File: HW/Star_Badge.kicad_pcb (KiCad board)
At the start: 2 copper layers, 180 x 171.6 mm, 55 parts, among them J1 AVR-ISP-6, J2 10118194-0001LF, Q1 Q_NMOS_DGS, Q2 Q_PMOS_DGS, U1 ATTINY861-15XD, U2 TPS613221ADBVT, U3 AP7363-33D-13, X1 Badgelife_sao_connector_v169b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, X2 Badgelife_sao_connector_v169b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, X3 Badgelife_sao_connector_v169b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

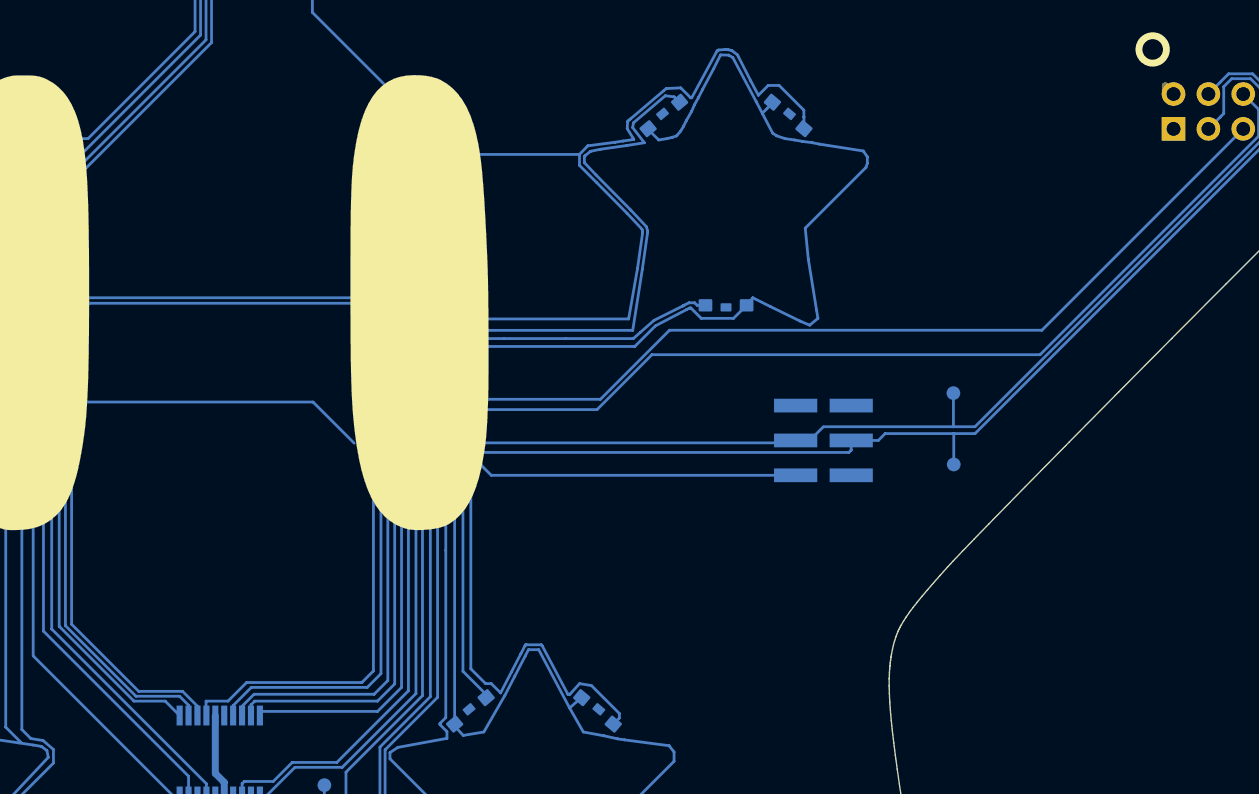
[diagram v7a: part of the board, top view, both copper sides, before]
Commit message: RESET wrired
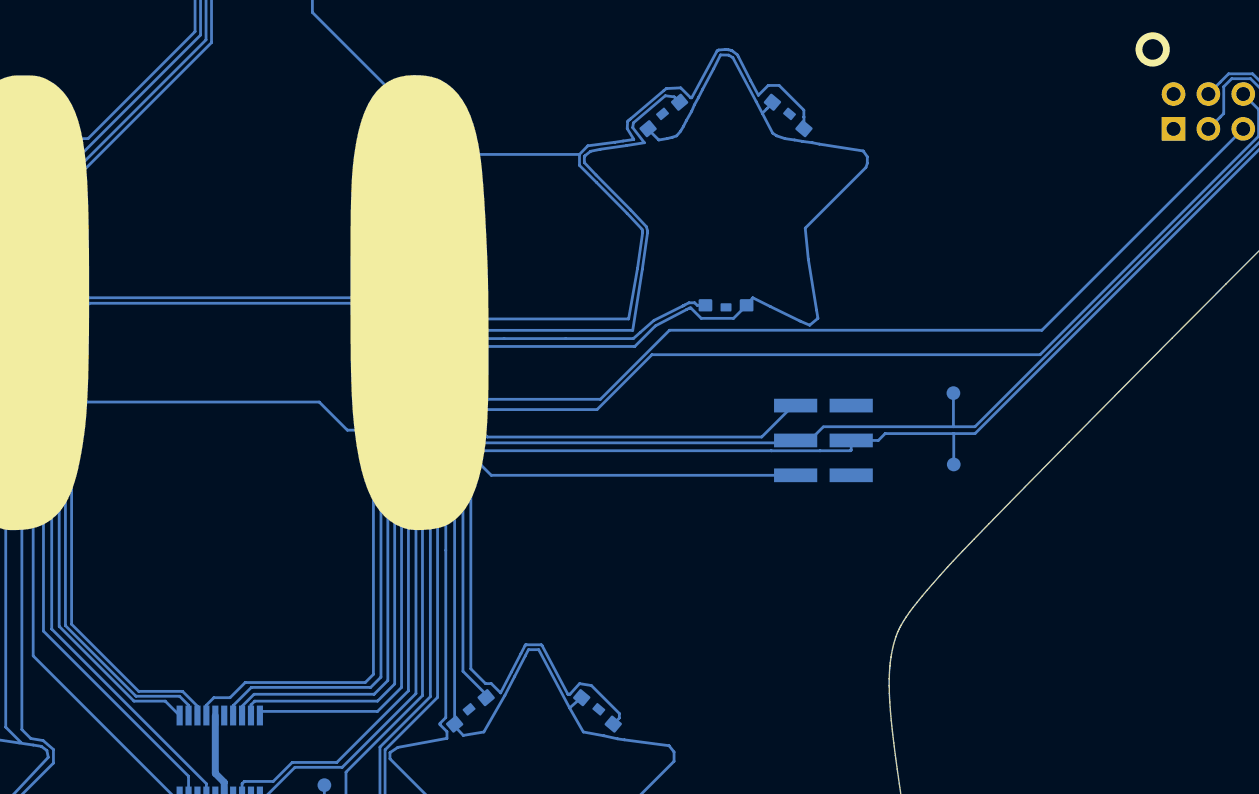
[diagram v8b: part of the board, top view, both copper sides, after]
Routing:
- net /~RESET: track 61.3 -> 94.3 mm, vias 2 -> 4
- net /VBUS: track 243.5 -> 242.2 mm
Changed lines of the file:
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@@
     (thickness 1.6)
     (drawings 611)
-    (tracks 895)
+    (tracks 912)
     (zones 0)
     (modules 55)
@@
   (via (at 117.1 106.4) (size 0.4) (drill 0.3) (layers F.Cu B.Cu) (net 7))
   (segment (start 117.118794 130.675879) (end 117.118794 106.518794) (width 0.2032) (layer B.Cu) (net 7))
-  (segment (start 100.975 130.05) (end 100.975 129.327909) (width 0.2032) (layer B.Cu) (net 7))
-  (segment (start 111.75 106.782842) (end 111.75 106.5) (width 0.2032) (layer B.Cu) (net 7))
   (segment (start 111.85 106.4) (end 111.75 106.5) (width 0.2032) (layer F.Cu) (net 7))
-  (segment (start 111.75 127) (end 111.75 106.782842) (width 0.2032) (layer B.Cu) (net 7))
   (via (at 111.75 106.5) (size 0.4) (drill 0.3) (layers F.Cu B.Cu) (net 7))
-  (segment (start 100.975 129.327909) (end 102.302908 128) (width 0.2032) (layer B.Cu) (net 7))
   (segment (start 117.1 106.4) (end 111.85 106.4) (width 0.2032) (layer F.Cu) (net 7))
-  (segment (start 110.75 128) (end 111.75 127) (width 0.2032) (layer B.Cu) (net 7))
-  (segment (start 102.302908 128) (end 110.75 128) (width 0.2032) (layer B.Cu) (net 7))
+  (segment (start 100.975 129.327909) (end 102.302908 128) (width 0.2032) (layer B.Cu) (net 7))
+  (segment (start 102.302908 128) (end 111 128) (width 0.2032) (layer B.Cu) (net 7))
+  (segment (start 111.75 106.782842) (end 111.75 106.5) (width 0.2032) (layer B.Cu) (net 7))
+  (segment (start 100.975 130.05) (end 100.975 129.327909) (width 0.2032) (layer B.Cu) (net 7))
+  (segment (start 111 128) (end 111.75 127.25) (width 0.2032) (layer B.Cu) (net 7))
+  (segment (start 111.75 127.25) (end 111.75 106.782842) (width 0.2032) (layer B.Cu) (net 7))
   (via (at 81.600002 103) (size 0.4) (drill 0.3) (layers F.Cu B.Cu) (net 8))
   (segment (start 70.425 100.525) (end 70.41127 102.077546) (width 0.2032) (layer B.Cu) (net 8))
@@
   (via (at 115.65 103.15) (size 0.4) (drill 0.3) (layers F.Cu B.Cu) (net 10))
   (segment (start 115.65 103.15) (end 111.2 103.15) (width 0.2032) (layer F.Cu) (net 10))
+  (segment (start 111.2 127.05) (end 111.2 103.482846) (width 0.2032) (layer B.Cu) (net 10))
   (segment (start 111.2 103.482846) (end 111.2 103.200004) (width 0.2032) (layer B.Cu) (net 10))
-  (segment (start 111.2 126.8) (end 111.2 103.482846) (width 0.2032) (layer B.Cu) (net 10))
-  (segment (start 110.35561 127.64439) (end 111.2 126.8) (width 0.2032) (layer B.Cu) (net 10))
-  (segment (start 101.95561 127.64439) (end 110.35561 127.64439) (width 0.2032) (layer B.Cu) (net 10))
-  (segment (start 100.6 129) (end 101.95561 127.64439) (width 0.2032) (layer B.Cu) (net 10))
-  (segment (start 99 129) (end 100.6 129) (width 0.2032) (layer B.Cu) (net 10))
-  (segment (start 99 129.672586) (end 99 129) (width 0.2032) (layer B.Cu) (net 10))
+  (segment (start 110.60561 127.64439) (end 111.2 127.05) (width 0.2032) (layer B.Cu) (net 10))
+  (segment (start 99 129.317798) (end 99.567798 128.75) (width 0.2032) (layer B.Cu) (net 10))
+  (segment (start 99 129.672586) (end 99 129.317798) (width 0.2032) (layer B.Cu) (net 10))
+  (segment (start 99.567798 128.75) (end 100.75 128.75) (width 0.2032) (layer B.Cu) (net 10))
+  (segment (start 100.75 128.75) (end 101.85561 127.64439) (width 0.2032) (layer B.Cu) (net 10))
+  (segment (start 101.85561 127.64439) (end 110.60561 127.64439) (width 0.2032) (layer B.Cu) (net 10))
   (segment (start 97.288778 128.288778) (end 98.375 129.375) (width 0.2032) (layer B.Cu) (net 11))
   (segment (start 94.088778 128.288778) (end 97.288778 128.288778) (width 0.2032) (layer B.Cu) (net 11))
@@
   (segment (start 100.325 135.95) (end 100.325 139.975) (width 0.508) (layer B.Cu) (net 15))
   (segment (start 100.325 139.975) (end 96.799999 143.500001) (width 0.508) (layer B.Cu) (net 15))
-  (segment (start 169.52 84.75) (end 168.92 84.15) (width 0.508) (layer F.Cu) (net 15))
-  (segment (start 168.92 84.15) (end 168.92 84.655) (width 0.508) (layer F.Cu) (net 15))
   (segment (start 99.953954 44.601814) (end 100.048186 44.601814) (width 0.508) (layer F.Cu) (net 15))
   (segment (start 26.383599 83.886401) (end 26.383599 79.691401) (width 0.508) (layer B.Cu) (net 15))
@@
   (segment (start 118.9 110.875) (end 118.9 110.875) (width 0.2032) (layer F.Cu) (net 17))
   (via (at 118.9 110.875) (size 0.4) (drill 0.3) (layers F.Cu B.Cu) (net 17))
-  (segment (start 146.025 110.7032) (end 146.025 110) (width 0.2032) (layer B.Cu) (net 17))
-  (segment (start 145.8532 110.875) (end 146.025 110.7032) (width 0.2032) (layer B.Cu) (net 17))
-  (segment (start 118.9 110.875) (end 145.8532 110.875) (width 0.2032) (layer B.Cu) (net 17))
   (via (at 114.3 111.325) (size 0.4) (drill 0.3) (layers F.Cu B.Cu) (net 17))
   (segment (start 114.75 110.875) (end 114.499999 111.125001) (width 0.2032) (layer F.Cu) (net 17))
@@
   (segment (start 147 110) (end 148 110) (width 0.2032) (layer B.Cu) (net 17))
   (segment (start 148 110) (end 148.5 109.5) (width 0.2032) (layer B.Cu) (net 17))
+  (segment (start 146.025 110.7032) (end 146.025 110) (width 0.2032) (layer B.Cu) (net 17))
+  (segment (start 145.9782 110.75) (end 146.025 110.7032) (width 0.2032) (layer B.Cu) (net 17))
+  (segment (start 143.757202 110.75) (end 145.9782 110.75) (width 0.2032) (layer B.Cu) (net 17))
+  (segment (start 143.753201 110.754001) (end 143.757202 110.75) (width 0.2032) (layer B.Cu) (net 17))
+  (segment (start 119.025 110.75) (end 140.192798 110.75) (width 0.2032) (layer B.Cu) (net 17))
+  (segment (start 118.9 110.875) (end 119.025 110.75) (width 0.2032) (layer B.Cu) (net 17))
+  (segment (start 140.192798 110.75) (end 140.196799 110.754001) (width 0.2032) (layer B.Cu) (net 17))
+  (segment (start 140.196799 110.754001) (end 143.753201 110.754001) (width 0.2032) (layer B.Cu) (net 17))
   (segment (start 97.075 138.05) (end 96.3 138.825) (width 0.508) (layer B.Cu) (net 18))
   (segment (start 97.075 135.95) (end 97.075 138.05) (width 0.508) (layer B.Cu) (net 18))
@@
   (segment (start 86.4 107.2) (end 89.8 107.2) (width 0.2032) (layer F.Cu) (net 18))
   (via (at 89.8 107.2) (size 0.4) (drill 0.3) (layers F.Cu B.Cu) (net 18))
-  (segment (start 109.8 110.2) (end 106.8 107.2) (width 0.2032) (layer B.Cu) (net 18))
   (segment (start 90.082842 107.2) (end 89.8 107.2) (width 0.2032) (layer B.Cu) (net 18))
-  (segment (start 106.8 107.2) (end 90.082842 107.2) (width 0.2032) (layer B.Cu) (net 18))
+  (segment (start 107.25 107.2) (end 90.082842 107.2) (width 0.2032) (layer B.Cu) (net 18))
+  (segment (start 110.5 109.25) (end 110.5 109.25) (width 0.2032) (layer B.Cu) (net 18))
+  (segment (start 109.3 109.25) (end 107.25 107.2) (width 0.2032) (layer B.Cu) (net 18))
+  (segment (start 110.5 109.25) (end 109.3 109.25) (width 0.2032) (layer B.Cu) (net 18))
+  (via (at 110.5 109.25) (size 0.4) (drill 0.3) (layers F.Cu B.Cu) (net 18))
+  (segment (start 110.5 109.25) (end 118.75 109.25) (width 0.2032) (layer F.Cu) (net 18))
+  (segment (start 118.75 109.25) (end 119 109.25) (width 0.2032) (layer F.Cu) (net 18))
+  (segment (start 119 109.25) (end 119 109.25) (width 0.2032) (layer F.Cu) (net 18))
+  (via (at 119 109.25) (size 0.4) (drill 0.3) (layers F.Cu B.Cu) (net 18))
+  (segment (start 119.5 109.75) (end 139.5 109.75) (width 0.2032) (layer B.Cu) (net 18))
+  (segment (start 119 109.25) (end 119.5 109.75) (width 0.2032) (layer B.Cu) (net 18))
+  (segment (start 141.975 107.475) (end 141.975 107.46) (width 0.2032) (layer B.Cu) (net 18))
+  (segment (start 139.5 109.75) (end 141.75 107.5) (width 0.2032) (layer B.Cu) (net 18))
+  (segment (start 141.75 107.5) (end 142 107.5) (width 0.2032) (layer B.Cu) (net 18))
+  (segment (start 142 107.5) (end 141.975 107.475) (width 0.2032) (layer B.Cu) (net 18))
   (segment (start 79.225 150.6) (end 79.2 150.625) (width 0.4572) (layer B.Cu) (net 19))
   (segment (start 83 150.6) (end 79.225 150.6) (width 0.4572) (layer B.Cu) (net 19))
